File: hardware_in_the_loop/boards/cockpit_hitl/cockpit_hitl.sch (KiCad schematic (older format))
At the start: 33 parts, among them J1 CONN_02X03, U1 MCP2561-E_SN, U101 TPS560430YF, U2 ATMEGA16M1, Y1 Crystal_SMD

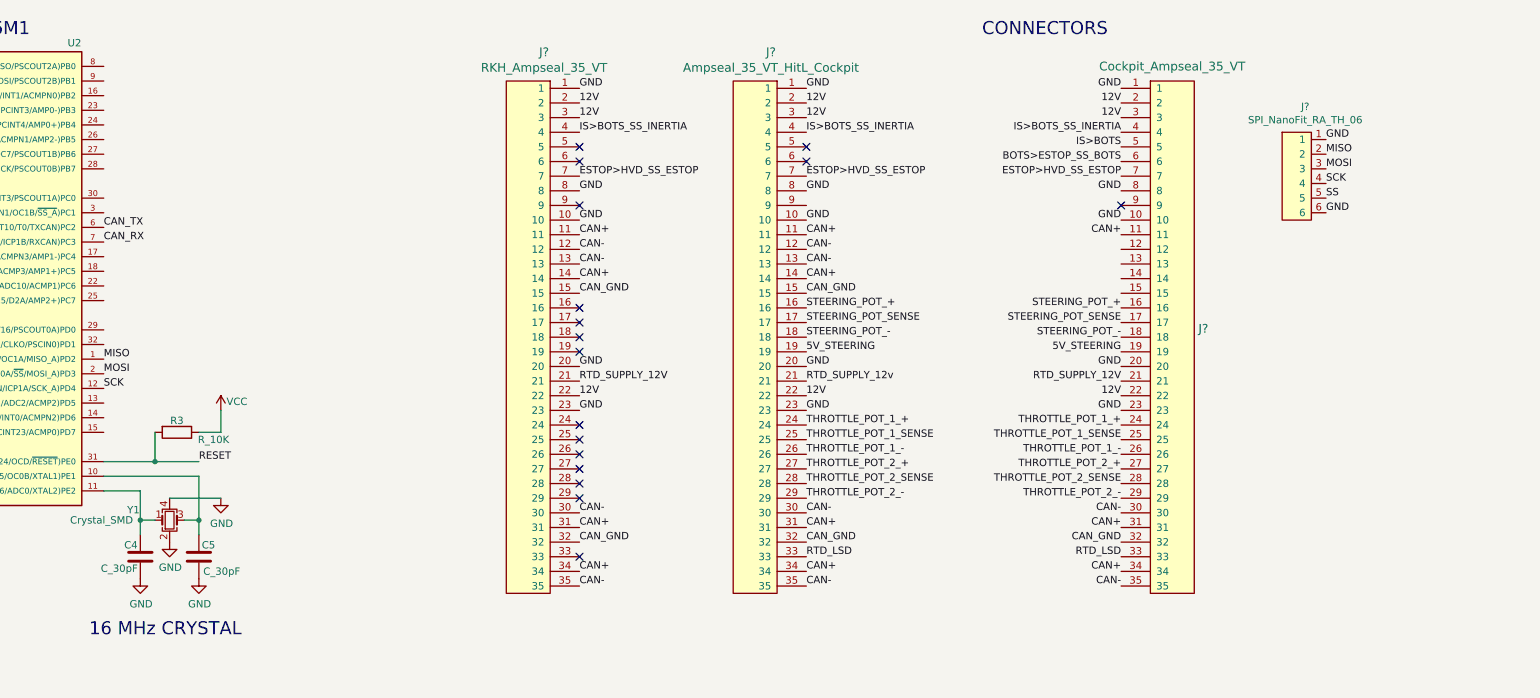
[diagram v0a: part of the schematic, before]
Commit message: Completed first draft of schematic
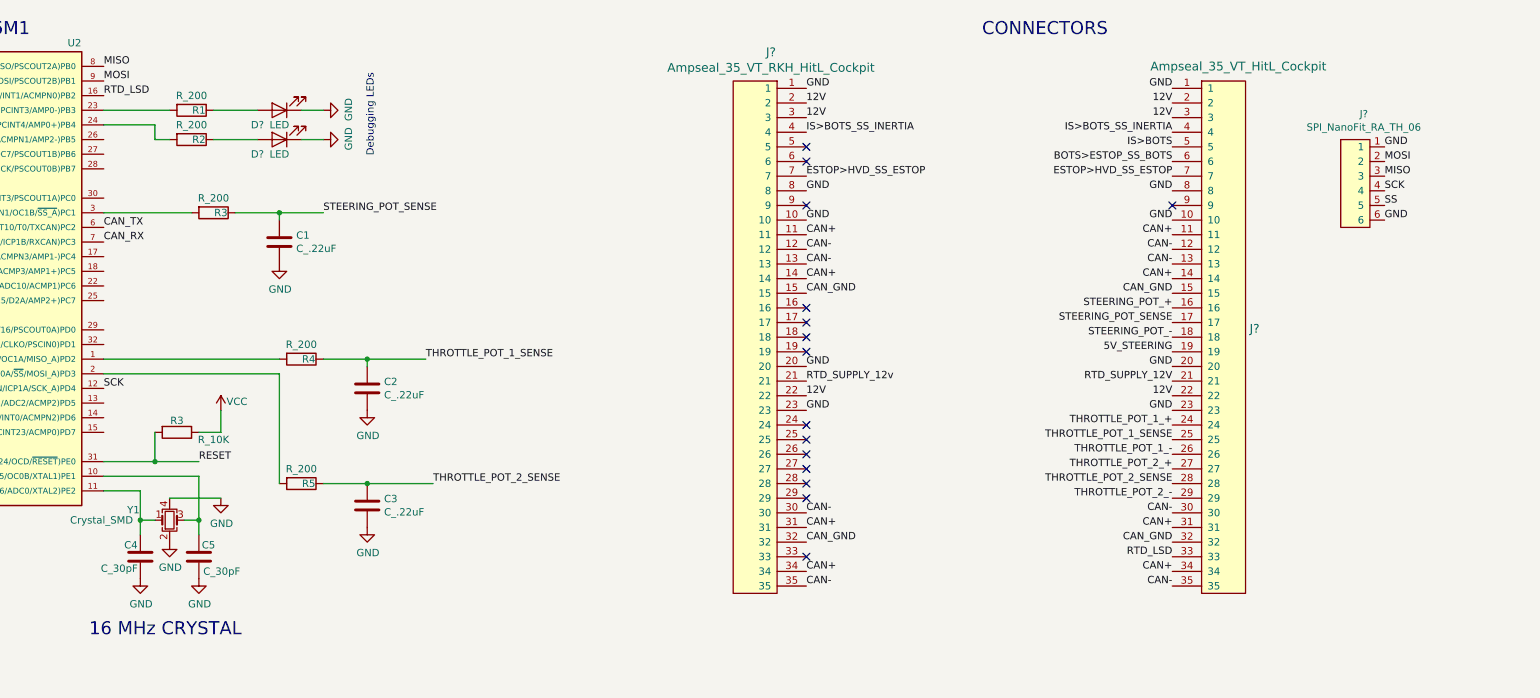
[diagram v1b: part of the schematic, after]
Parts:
- removed J?: RKH_Ampseal_35_VT, footprints:Ampseal_35, symbol formula:Ampseal_35_VT
- added C1, C2, C3: C_.22uF, footprints:C_0805_OEM, symbol formula:C_.22uF
- added D? (x2): LED, footprints:LED_0805_OEM, symbol formula:LED_0805
- added R1, R2, R3, R4, R5: R_200, footprints:R_0805_OEM, symbol formula:R_200
- J?: value Cockpit_Ampseal_35_VT -> Ampseal_35_VT_HitL_Cockpit
- J?: value Ampseal_35_VT_HitL_Cockpit -> Ampseal_35_VT_RKH_HitL_Cockpit
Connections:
- net 5V_STEERING: no longer J?.19
- net CAN+: now also J?.14
- net CAN-: now also J?.12, J?.13
- net CAN_GND: now also J?.15
- net GND: now also C1.2, C2.2, C3.2, D?.1 (K), D?.1 (K)
- net MISO: now also J?.3, U2.8 ((PCINT0/MISO/PSCOUT2A)PB0); no longer J?.2, U2.1 ((PCINT18/PSCIN2/OC1A/MISO_A)PD2)
- net MOSI: now also J?.2, U2.9 ((PCINT1/MOSI/PSCOUT2B)PB1); no longer J?.3, U2.2 ((PCINT19/TXD/TXLIN/OC0A/~SS~/MOSI_A)PD3)
- net RTD_LSD: now also U2.16 ((PCINT2/ADC5/INT1/ACMPN0)PB2); no longer J?.33
- net STEERING_POT_+: no longer J?.16
- net STEERING_POT_-: no longer J?.18
- net STEERING_POT_SENSE: now also C1.1, R3.1; no longer J?.17
- net THROTTLE_POT_1_+: no longer J?.24
- net THROTTLE_POT_1_-: no longer J?.26
- net THROTTLE_POT_1_SENSE: now also C2.1, R4.1; no longer J?.25
- net THROTTLE_POT_2_+: no longer J?.27
- net THROTTLE_POT_2_-: no longer J?.29
- net THROTTLE_POT_2_SENSE: now also C3.1, R5.1; no longer J?.28
- net at U2.23 ((PCINT3/AMP0-)PB3): now also R1.2
- net at U2.24 ((PCINT4/AMP0+)PB4): now also R2.2
- net at U2.3 ((PCINT9/PSCIN1/OC1B/~SS_A~)PC1): now also R3.2
- new net: R4.2, U2.1 ((PCINT18/PSCIN2/OC1A/MISO_A)PD2)
- new net: R5.2, U2.2 ((PCINT19/TXD/TXLIN/OC0A/~SS~/MOSI_A)PD3)
- new net: D?.2 (A), R1.1
- new net: D?.2 (A), R2.1
- no-connect marks 19 -> 17
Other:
- note added: "Debugging LEDs"
- moved on the sheet: J?

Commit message: some relabeling and formatting
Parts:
- removed C1, C2, C3: C_.22uF, footprints:C_0805_OEM, symbol formula:C_.22uF
- removed R1, R2, R3, R4, R5: R_200, footprints:R_0805_OEM, symbol formula:R_200
- added C? (x3): C_.22uF, footprints:C_0805_OEM, symbol formula:C_.22uF
- added R? (x5): R_200, footprints:R_0805_OEM, symbol formula:R_200
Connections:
- net CAN+ is gone; now on net CAN_HI: J?.11, J?.11, J?.14, J?.14, J?.31, J?.31, J?.34, J?.34
- net CAN- is gone; now on net CAN_LO: J?.12, J?.12, J?.13, J?.13, J?.30, J?.30, J?.35, J?.35
- net RTD_SUPPLY_12V is gone; now on net 12V: J?.21
- net RTD_SUPPLY_12v is gone; now on net 12V: J?.21
- net GND: now also C?.2, C?.2, C?.2
- net STEERING_POT_SENSE: now also C?.1, R?.1
- net THROTTLE_POT_1_SENSE: now also C?.1, R?.1
- net THROTTLE_POT_2_SENSE: now also C?.1, R?.1
- net at U2.1 ((PCINT18/PSCIN2/OC1A/MISO_A)PD2): now also R?.2
- net at U2.2 ((PCINT19/TXD/TXLIN/OC0A/~SS~/MOSI_A)PD3): now also R?.2
- net at U2.23 ((PCINT3/AMP0-)PB3): now also R?.2
- net at U2.24 ((PCINT4/AMP0+)PB4): now also R?.2
- net at U2.3 ((PCINT9/PSCIN1/OC1B/~SS_A~)PC1): now also R?.2
- net at D?.2 (A): now also R?.1 (x2)
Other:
- note added: "HitL ampseal connected to DUX Interface ampseal"
- note added: "HitL ampseal connected to RKH ampseal"
- note added: "R and C are placeholders"
- note added: "SHUTDOWN CIRCUIT"
- note added: "SPI Connector\n"
- moved on the sheet: C1, C101, C102, C103, C2, C3, C4, C5, COUT101, COUT102, COUT103, D101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

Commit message: added some labels
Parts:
- C1, C101, C103, C2: symbol template-rescue:C_0.1uF-formula -> cockpit_hitl-rescue:C_0.1uF-formula-template-rescue
- C102: symbol template-rescue:C_2.2uF-formula -> cockpit_hitl-rescue:C_2.2uF-formula-template-rescue
- C3: symbol template-rescue:C_100pF-formula -> cockpit_hitl-rescue:C_100pF-formula-template-rescue
- C4, C5: symbol template-rescue:C_30pF-formula -> cockpit_hitl-rescue:C_30pF-formula-template-rescue
- COUT101: symbol template-rescue:C_22uF-formula -> cockpit_hitl-rescue:C_22uF-formula-template-rescue
- COUT102: symbol template-rescue:C_33uF-formula -> cockpit_hitl-rescue:C_33uF-formula-template-rescue
- COUT103: symbol template-rescue:C_47uF-formula -> cockpit_hitl-rescue:C_47uF-formula-template-rescue
- D101: symbol template-rescue:D_Zener_18V-formula -> cockpit_hitl-rescue:D_Zener_18V-formula-template-rescue
- D102, D103: symbol template-rescue:LED_0805-formula -> cockpit_hitl-rescue:LED_0805-formula-template-rescue
- F101: symbol template-rescue:F_500mA_16V-formula -> cockpit_hitl-rescue:F_500mA_16V-formula-template-rescue
- J1: symbol template-rescue:CONN_02X03-formula -> cockpit_hitl-rescue:CONN_02X03-formula-template-rescue
- L101: symbol template-rescue:L_100uH-formula -> cockpit_hitl-rescue:L_100uH-formula-template-rescue
- R1: symbol template-rescue:R_100-formula -> cockpit_hitl-rescue:R_100-formula-template-rescue
- R102: symbol template-rescue:R_25K-formula -> cockpit_hitl-rescue:R_25K-formula-template-rescue
- R103: symbol template-rescue:R_100K-formula -> cockpit_hitl-rescue:R_100K-formula-template-rescue
- R104: symbol template-rescue:R_0_2512-formula -> cockpit_hitl-rescue:R_0_2512-formula-template-rescue
- R105, R2: symbol template-rescue:R_200-formula -> cockpit_hitl-rescue:R_200-formula-template-rescue
- R3: symbol template-rescue:R_10K-formula -> cockpit_hitl-rescue:R_10K-formula-template-rescue
- U1: symbol template-rescue:MCP2561-E_SN-formula -> cockpit_hitl-rescue:MCP2561-E_SN-formula-template-rescue
- U101: symbol template-rescue:TPS560430YF-formula -> cockpit_hitl-rescue:TPS560430YF-formula-template-rescue
- U2: symbol template-rescue:ATMEGA16M1-formula -> cockpit_hitl-rescue:ATMEGA16M1-formula-template-rescue
- Y1: symbol template-rescue:Crystal_SMD-formula -> cockpit_hitl-rescue:Crystal_SMD-formula-template-rescue
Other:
- note added: "add pull-up resistor"
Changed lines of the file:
@@
 $EndComp
 $Comp
-L template-rescue:C_2.2uF-formula C102
+L cockpit_hitl-rescue:C_2.2uF-formula-template-rescue C102
 U 1 1 5BEE2647
 P 2500 8800
@@
 $EndComp
 $Comp
-L template-rescue:C_0.1uF-formula C101
+L cockpit_hitl-rescue:C_0.1uF-formula-template-rescue C101
 U 1 1 5BEE2923
 P 2200 8800
@@
 $EndComp
 $Comp
-L template-rescue:R_100K-formula R103
+L cockpit_hitl-rescue:R_100K-formula-template-rescue R103
 U 1 1 5BEE2A52
 P 4100 9450
@@
 $EndComp
 $Comp
-L template-rescue:C_0.1uF-formula C103
+L cockpit_hitl-rescue:C_0.1uF-formula-template-rescue C103
 U 1 1 5BEE239B
 P 4100 8600
@@
 12V
 $Comp
-L template-rescue:C_22uF-formula COUT101
+L cockpit_hitl-rescue:C_22uF-formula-template-rescue COUT101
 U 1 1 5C061BB4
 P 4900 8900
@@
 $EndComp
 $Comp
-L template-rescue:C_47uF-formula COUT103
+L cockpit_hitl-rescue:C_47uF-formula-template-rescue COUT103
 U 1 1 5C062E7A
 P 5700 8900
@@
 $EndComp
 $Comp
-L template-rescue:C_33uF-formula COUT102
+L cockpit_hitl-rescue:C_33uF-formula-template-rescue COUT102
 U 1 1 5C08921B
 P 5300 8900
@@
 $EndComp
 $Comp
-L template-rescue:R_25K-formula R102
+L cockpit_hitl-rescue:R_25K-formula-template-rescue R102
 U 1 1 5C0B315C
 P 3600 9450
@@
 $EndComp
 $Comp
-L template-rescue:F_500mA_16V-formula F101
+L cockpit_hitl-rescue:F_500mA_16V-formula-template-rescue F101
 U 1 1 5C0BFA29
 P 1150 8650
@@
 $EndComp
 $Comp
-L template-rescue:R_0_2512-formula R104
+L cockpit_hitl-rescue:R_0_2512-formula-template-rescue R104
 U 1 1 5C0C29A9
 P 6250 8750
@@
 $EndComp
 $Comp
-L template-rescue:LED_0805-formula D103
+L cockpit_hitl-rescue:LED_0805-formula-template-rescue D103
 U 1 1 5C0C344A
 P 6650 9600
@@
 $EndComp
 $Comp
-L template-rescue:R_200-formula R105
+L cockpit_hitl-rescue:R_200-formula-template-rescue R105
 U 1 1 5C0C44F9
 P 6650 9000
@@
 $EndComp
 $Comp
-L template-rescue:D_Zener_18V-formula D101
+L cockpit_hitl-rescue:D_Zener_18V-formula-template-rescue D101
 U 1 1 5C623D49
 P 1400 8950
@@
 12V
 $Comp
-L template-rescue:LED_0805-formula D102
+L cockpit_hitl-rescue:LED_0805-formula-template-rescue D102
 U 1 1 5C754D7D
 P 1800 9200
@@
 5V Indicator
 $Comp
-L template-rescue:ATMEGA16M1-formula U2
+L cockpit_hitl-rescue:ATMEGA16M1-formula-template-rescue U2
 U 1 1 5D58A7A6
 P 2700 3200
@@
 RESET
 $Comp
-L template-rescue:R_100-formula R1
+L cockpit_hitl-rescue:R_100-formula-template-rescue R1
 U 1 1 5D58E16F
 P 1300 1650
@@
 $EndComp
 $Comp
-L template-rescue:C_100pF-formula C3
+L cockpit_hitl-rescue:C_100pF-formula-template-rescue C3
 U 1 1 5D58E505
 P 1300 1950
@@
 $EndComp
 $Comp
-L template-rescue:Crystal_SMD-formula Y1
+L cockpit_hitl-rescue:Crystal_SMD-formula-template-rescue Y1
 U 1 1 5D5EB332
 P 4250 4600
@@
 $EndComp
 $Comp
-L template-rescue:C_30pF-formula C4
+L cockpit_hitl-rescue:C_30pF-formula-template-rescue C4
 U 1 1 5D5EB5B2
 P 4050 4850
@@
 $EndComp
 $Comp
-L template-rescue:C_30pF-formula C5
+L cockpit_hitl-rescue:C_30pF-formula-template-rescue C5
 U 1 1 5D5EB694
 P 4450 4850
@@
 $EndComp
 $Comp
-L template-rescue:R_10K-formula R3
+L cockpit_hitl-rescue:R_10K-formula-template-rescue R3
 U 1 1 5D5EB7F3
 P 4300 4000
@@
 $EndComp
 $Comp
-L template-rescue:MCP2561-E_SN-formula U1
+L cockpit_hitl-rescue:MCP2561-E_SN-formula-template-rescue U1
 U 1 1 5D5FAEDE
 P 14850 2000
@@
 $EndComp
 $Comp
-L template-rescue:C_0.1uF-formula C1
+L cockpit_hitl-rescue:C_0.1uF-formula-template-rescue C1
 U 1 1 5D5FB603
 P 14700 1400
@@
 $EndComp
 $Comp
-L template-rescue:R_200-formula R2
+L cockpit_hitl-rescue:R_200-formula-template-rescue R2
 U 1 1 5D5FB79E
 P 15650 2000
@@
 GND
 $Comp
-L template-rescue:CONN_02X03-formula J1
+L cockpit_hitl-rescue:CONN_02X03-formula-template-rescue J1
 U 1 1 5D628C9D
 P 14850 3400
@@
 Connection ~ 1300 1800
 $Comp
-L template-rescue:C_0.1uF-formula C2
+L cockpit_hitl-rescue:C_0.1uF-formula-template-rescue C2
 U 1 1 5D58E34B
 P 950 1650
@@
 	900  8350 900  8650
 $Comp
-L template-rescue:TPS560430YF-formula U101
+L cockpit_hitl-rescue:TPS560430YF-formula-template-rescue U101
 U 1 1 5C75D405
 P 3200 8800
@@
 $EndComp
 $Comp
-L template-rescue:L_100uH-formula L101
+L cockpit_hitl-rescue:L_100uH-formula-template-rescue L101
 U 1 1 5F881F17
 P 4500 8750
@@
 Text Label 5300 2500 0    50   ~ 0
 STEERING_POT_SENSE
-Text Label 3850 1700 0    50   ~ 0
+Text Label 6950 1300 0    50   ~ 0
 RTD_LSD
 Text Notes 5650 1550 3    50   ~ 0
@@
 Wire Wire Line
 	5600 4350 6050 4350
-Wire Wire Line
-	3850 1700 3800 1700
 Text Notes 5500 2750 0    50   ~ 0
 R and C are placeholders
 Text Notes 6100 3750 0    50   ~ 0
 R and C are placeholders
-$Comp
-L power:VCC #PWR?
-U 1 1 5FB6AAAB
-P 6950 1300
-F 0 "#PWR?" H 6950 1150 50  0001 C CNN
-F 1 "VCC" H 6965 1473 50  0000 C CNN
-F 2 "" H 6950 1300 50  0001 C CNN
-F 3 "" H 6950 1300 50  0001 C CNN
-	1    6950 1300
-	1    0    0    -1
-$EndComp
 Text Notes 6050 4600 0    50   ~ 0
 R and C are placeholders
@@
 	13650 4250 13650 5100
 Wire Wire Line
-	6950 1800 6950 1950
-$Comp
-L power:GND #PWR?
-U 1 1 5FDA4807
-P 6950 1950
-F 0 "#PWR?" H 6950 1700 50  0001 C CNN
-F 1 "GND" H 6955 1777 50  0000 C CNN
-F 2 "" H 6950 1950 50  0001 C CNN
-F 3 "" H 6950 1950 50  0001 C CNN
-	1    6950 1950
-	1    0    0    -1
-$EndComp
+	4150 1300 6950 1300
+Wire Wire Line
+	3800 1700 4150 1700
+Wire Wire Line
+	4150 1300 4150 1700
+Text Notes 6550 1400 0    50   ~ 0
+add pull-up resistor
 $EndSCHEMATC
